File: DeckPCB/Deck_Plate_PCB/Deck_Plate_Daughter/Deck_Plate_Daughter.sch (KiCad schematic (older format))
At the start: 36 parts, among them J1 SunnyBuddy_Inhibit, J2 JST_Batt_Conn, J3 Motor_Inhibit, J4 BurnWire_Inhibit, J5 Power, J6 Raspberry_Pi_2_3, J7 Board_to_Board, Q1 Device_Q_NPN_BCE, U2 SunnyBuddy_Breakout, U3 Big_Easy_Driver, U4 TTL_Camera, U5 Adafruit_INA219_Breakout

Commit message: Started routing of Deck_Plate_PCB, the main board.
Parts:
- removed R4, R5: 10K, Resistor_THT:R_Axial_DIN0207_L6.3mm_D2.5mm_P10.16mm_Horizontal, symbol Device:R
- removed U4: TTL_Camera, Connector_PinHeader_2.54mm:PinHeader_1x04_P2.54mm_Vertical, symbol Deck_Plate_PCB:TTL_Camera
- J7: footprint Connector_PinHeader_2.54mm:PinHeader_1x07_P2.54mm_Vertical -> Connector_PinHeader_2.54mm:PinHeader_1x09_P2.54mm_Vertical; symbol Connector:Conn_01x07_Male -> Connector:Conn_01x09_Male
- Q1: value Device_Q_NPN_BCE -> BurnWire; symbol Deck_Plate_PCB-cache:Device_Q_NPN_BCE -> Deck_Plate_Daughter-rescue:Device_Q_NPN_BCE-Deck_Plate_PCB-cache
- U2: symbol Deck_Plate_PCB-cache:Deck_Plate_PCB_SunnyBuddy_Breakout -> Deck_Plate_Daughter-rescue:Deck_Plate_PCB_SunnyBuddy_Breakout-Deck_Plate_PCB-cache
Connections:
- net labels added: PayloadTemp, SCL, SDA, SolarArrayTemp
- net labels removed: 20(SDA), 21(SCL)
- wire segments 66 -> 59
- no-connect marks 20 -> 22
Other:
- note added: "BurnWire Circuitry"
- note added: "Inhibit Circuitry"
- note added: "RaspberryPI Interface"
- note added: "Signal and Power Board-to-Board Transfer"
- note added: "Solar Panel and Sensor Mangement"
- note removed: "TODO: Remove TTL camera back to other board and add 10k resistor connections to Arduino"
- moved on the sheet: D1, H15, H16, H17, H18, J1, J2, J3, J4, J5, J6, R1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

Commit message: Finised routing fro Main_Board, Daughter_Board, and BurnWire circuits. Creating SensorEndPanel board next.
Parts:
- removed Q1: BurnWire, Package_TO_SOT_THT:TO-251-3_Vertical, symbol Deck_Plate_Daughter-rescue:Device_Q_NPN_BCE-Deck_Plate_PCB-cache
- removed R2, R3: 4.7, Resistor_THT:R_Axial_DIN0207_L6.3mm_D2.5mm_P10.16mm_Horizontal, symbol Device:R
- J4: footprint Connector_PinHeader_2.54mm:PinHeader_1x02_P2.54mm_Vertical -> Connector_PinHeader_2.54mm:PinHeader_1x05_P2.54mm_Vertical; symbol Connector:Conn_01x02_Male -> Connector:Conn_01x05_Male
- J5: footprint Connector_PinHeader_2.54mm:PinHeader_1x03_P2.54mm_Vertical -> Connector_PinHeader_2.54mm:PinHeader_1x04_P2.54mm_Vertical; symbol Connector:Conn_01x03_Male -> Connector:Conn_01x04_Male
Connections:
- net Solar_IN- is gone; now on net GND: U2.1 (Solar_IN-)
- net 5V_Bus_1: now also J4.2 (Pin_2)
- net BurnWireSignal: now also J4.4 (Pin_4), J4.5 (Pin_5); no longer J4.2 (Pin_2)
- net GND: now also J1.3 (Pin_3), J4.3 (Pin_3), J5.4 (Pin_4); no longer J1.1 (Pin_1), J1.4 (Pin_4)
- net Sunny_Batt_Out: now also J1.1 (Pin_1), J1.4 (Pin_4); no longer J1.3 (Pin_3)
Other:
- note removed: "BurnWire Circuitry"
- moved on the sheet: J7
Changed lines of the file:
@@
 Wire Wire Line
 	1300 1200 1150 1200
-Text Label 1150 900  2    50   ~ 0
-Solar_IN-
 Text Label 1150 1000 2    50   ~ 0
 Solar_IN+
@@
 $EndComp
 Text Label 3000 1400 0    50   ~ 0
-5V_Bus_1
-$Comp
-L Deck_Plate_Daughter-rescue:Device_Q_NPN_BCE-Deck_Plate_PCB-cache Q1
-U 1 1 5E6100C5
-P 1450 3550
-F 0 "Q1" H 1641 3596 50  0000 L CNN
-F 1 "BurnWire" H 1641 3505 50  0000 L CNN
-F 2 "Package_TO_SOT_THT:TO-251-3_Vertical" H 1650 3650 50  0001 C CNN
-F 3 "" H 1450 3550 50  0001 C CNN
-	1    1450 3550
-	1    0    0    -1
-$EndComp
-$Comp
-L Device:R R2
-U 1 1 5E610D52
-P 1350 4000
-F 0 "R2" H 1420 4046 50  0000 L CNN
-F 1 "4.7" H 1420 3955 50  0000 L CNN
-F 2 "Resistor_THT:R_Axial_DIN0207_L6.3mm_D2.5mm_P10.16mm_Horizontal" V 1280 4000 50  0001 C CNN
-F 3 "~" H 1350 4000 50  0001 C CNN
-	1    1350 4000
-	1    0    0    -1
-$EndComp
-$Comp
-L Device:R R3
-U 1 1 5E611957
-P 1750 4000
-F 0 "R3" H 1820 4046 50  0000 L CNN
-F 1 "4.7" H 1820 3955 50  0000 L CNN
-F 2 "Resistor_THT:R_Axial_DIN0207_L6.3mm_D2.5mm_P10.16mm_Horizontal" V 1680 4000 50  0001 C CNN
-F 3 "~" H 1750 4000 50  0001 C CNN
-	1    1750 4000
-	1    0    0    -1
-$EndComp
-Wire Wire Line
-	1550 3750 1550 3850
-Wire Wire Line
-	1550 3850 1750 3850
-Wire Wire Line
-	1550 3850 1350 3850
-Connection ~ 1550 3850
-Wire Wire Line
-	1350 4150 1350 4200
-Wire Wire Line
-	1350 4200 1550 4200
-Wire Wire Line
-	1750 4200 1750 4150
-$Comp
-L power:GND #PWR0103
-U 1 1 5E61DCB1
-P 1550 4200
-F 0 "#PWR0103" H 1550 3950 50  0001 C CNN
-F 1 "GND" H 1555 4027 50  0000 C CNN
-F 2 "" H 1550 4200 50  0001 C CNN
-F 3 "" H 1550 4200 50  0001 C CNN
-	1    1550 4200
-	1    0    0    -1
-$EndComp
-Connection ~ 1550 4200
-Wire Wire Line
-	1550 4200 1750 4200
-Text Label 1250 3550 2    50   ~ 0
-BurnWireSignal
-Wire Wire Line
-	1550 3350 1550 3150
-Text Label 1550 3150 0    50   ~ 0
 5V_Bus_1
 $Comp
@@
 U 1 1 5E692559
 P 5500 950
-F 0 "J1" V 5800 1000 50  0000 L CNN
-F 1 "SunnyBuddy_Inhibit" V 5450 700 50  0000 L CNN
+F 0 "J1" V 5950 1100 50  0000 L CNN
+F 1 "SunnyBuddy_Inhibit" V 5450 600 50  0000 L CNN
 F 2 "Connector_PinHeader_2.54mm:PinHeader_1x04_P2.54mm_Vertical" H 5500 950 50  0001 C CNN
 F 3 "~" H 5500 950 50  0001 C CNN
@@
 $EndComp
 $Comp
-L power:GND #PWR0109
-U 1 1 5E693738
-P 5300 1150
-F 0 "#PWR0109" H 5300 900 50  0001 C CNN
-F 1 "GND" V 5305 1022 50  0000 R CNN
-F 2 "" H 5300 1150 50  0001 C CNN
-F 3 "" H 5300 1150 50  0001 C CNN
-	1    5300 1150
-	0    1    1    0
-$EndComp
-$Comp
 L power:GND #PWR0110
 U 1 1 5E693E04
-P 5600 1150
-F 0 "#PWR0110" H 5600 900 50  0001 C CNN
-F 1 "GND" V 5605 1022 50  0000 R CNN
-F 2 "" H 5600 1150 50  0001 C CNN
-F 3 "" H 5600 1150 50  0001 C CNN
-	1    5600 1150
-	0    -1   -1   0
+P 5400 1250
+F 0 "#PWR0110" H 5400 1000 50  0001 C CNN
+F 1 "GND" V 5405 1122 50  0000 R CNN
+F 2 "" H 5400 1250 50  0001 C CNN
+F 3 "" H 5400 1250 50  0001 C CNN
+	1    5400 1250
+	1    0    0    -1
 $EndComp
 Wire Wire Line
@@
 Wire Wire Line
 	5500 1150 5500 1250
-Text Label 5400 1250 3    50   ~ 0
+Text Label 5300 1250 3    50   ~ 0
 Sunny_Batt_Out
 Text Label 5500 1250 3    50   ~ 0
@@
 9V_Bus
 $Comp
-L Connector:Conn_01x02_Male J4
+L Connector:Conn_01x05_Male J4
 U 1 1 5E6B7185
 P 7750 950
-F 0 "J4" V 8100 1000 50  0000 L CNN
+F 0 "J4" V 8100 1350 50  0000 L CNN
 F 1 "BurnWire_Inhibit" V 7700 800 50  0000 L CNN
-F 2 "Connector_PinHeader_2.54mm:PinHeader_1x02_P2.54mm_Vertical" H 7750 950 50  0001 C CNN
+F 2 "Connector_PinHeader_2.54mm:PinHeader_1x05_P2.54mm_Vertical" H 7750 950 50  0001 C CNN
 F 3 "~" H 7750 950 50  0001 C CNN
 	1    7750 950
@@
 $EndComp
 Wire Wire Line
-	7650 1150 7650 1250
-Wire Wire Line
 	7750 1150 7750 1250
-Text Label 7650 1250 3    50   ~ 0
+Text Label 7550 1150 3    50   ~ 0
 BurnWireSignal
-Text Label 7750 1250 3    50   ~ 0
+Text Label 7650 1150 3    50   ~ 0
 BurnWireSignal
 $Comp
-L Connector:Conn_01x03_Male J5
+L Connector:Conn_01x04_Male J5
 U 1 1 5E6C52D2
-P 4100 3650
-F 0 "J5" H 4400 3500 50  0000 L CNN
-F 1 "Power" H 4050 3850 50  0000 L CNN
-F 2 "Connector_PinHeader_2.54mm:PinHeader_1x03_P2.54mm_Vertical" H 4100 3650 50  0001 C CNN
-F 3 "~" H 4100 3650 50  0001 C CNN
-	1    4100 3650
-	1    0    0    -1
-$EndComp
-Wire Wire Line
-	4300 3750 4400 3750
-Wire Wire Line
-	4300 3550 4400 3550
-Wire Wire Line
-	4300 3650 4400 3650
-Text Label 4400 3550 0    50   ~ 0
+P 750 4500
+F 0 "J5" H 750 4200 50  0000 L CNN
+F 1 "Power" H 700 4700 50  0000 L CNN
+F 2 "Connector_PinHeader_2.54mm:PinHeader_1x04_P2.54mm_Vertical" H 750 4500 50  0001 C CNN
+F 3 "~" H 750 4500 50  0001 C CNN
+	1    750  4500
+	1    0    0    -1
+$EndComp
+Wire Wire Line
+	950  4600 1050 4600
+Wire Wire Line
+	950  4400 1050 4400
+Wire Wire Line
+	950  4500 1050 4500
+Text Label 1050 4400 0    50   ~ 0
 5V_Bus_1
-Text Label 4400 3650 0    50   ~ 0
+Text Label 1050 4500 0    50   ~ 0
 9V_Bus
-Text Label 4400 3750 0    50   ~ 0
+Text Label 1050 4600 0    50   ~ 0
 5V_Bus_2
 $Comp
@@
 L Connector:Conn_01x09_Male J7
 U 1 1 5EDC5910
-P 4100 2850
-F 0 "J7" H 4450 2400 50  0000 C CNN
-F 1 "Board_to_Board" H 4350 3400 50  0000 C CNN
-F 2 "Connector_PinHeader_2.54mm:PinHeader_1x09_P2.54mm_Vertical" H 4100 2850 50  0001 C CNN
-F 3 "~" H 4100 2850 50  0001 C CNN
-	1    4100 2850
-	1    0    0    -1
-$EndComp
-Wire Wire Line
-	4300 2650 4400 2650
-Wire Wire Line
-	4300 2750 4400 2750
-Wire Wire Line
-	4300 2850 4400 2850
-Wire Wire Line
-	4300 2950 4400 2950
-Wire Wire Line
-	4300 3050 4400 3050
-Text Label 4400 2650 0    50   ~ 0
+P 750 3700
+F 0 "J7" H 1100 3250 50  0000 C CNN
+F 1 "Board_to_Board" H 1000 4250 50  0000 C CNN
+F 2 "Connector_PinHeader_2.54mm:PinHeader_1x09_P2.54mm_Vertical" H 750 3700 50  0001 C CNN
+F 3 "~" H 750 3700 50  0001 C CNN
+	1    750  3700
+	1    0    0    -1
+$EndComp
+Wire Wire Line
+	950  3500 1050 3500
+Wire Wire Line
+	950  3600 1050 3600
+Wire Wire Line
+	950  3700 1050 3700
+Wire Wire Line
+	950  3800 1050 3800
+Wire Wire Line
+	950  3900 1050 3900
+Text Label 1050 3500 0    50   ~ 0
 TTL_TX
-Text Label 4400 2750 0    50   ~ 0
+Text Label 1050 3600 0    50   ~ 0
 TTL_RX
-Text Label 4400 2850 0    50   ~ 0
+Text Label 1050 3700 0    50   ~ 0
 BurnWireSignal
-Text Label 4400 2950 0    50   ~ 0
+Text Label 1050 3800 0    50   ~ 0
 Step
-Text Label 4400 3050 0    50   ~ 0
+Text Label 1050 3900 0    50   ~ 0
 Dir
 Wire Wire Line
-	4300 3150 4400 3150
-Wire Wire Line
-	4300 2550 4400 2550
-Text Label 4400 2450 0    50   ~ 0
+	950  4000 1050 4000
+Wire Wire Line
+	950  3400 1050 3400
+Text Label 1050 3300 0    50   ~ 0
 SDA
-Text Label 4400 2550 0    50   ~ 0
+Text Label 1050 3400 0    50   ~ 0
 SCL
 $Comp
@@
 $EndComp
 Wire Wire Line
-	4300 2450 4400 2450
-Wire Wire Line
-	4300 3250 4400 3250
-Text Label 4400 3150 0    50   ~ 0
+	950  3300 1050 3300
+Wire Wire Line
+	950  4100 1050 4100
+Text Label 1050 4000 0    50   ~ 0
 SolarArrayTemp
-Text Label 4400 3250 0    50   ~ 0
+Text Label 1050 4100 0    50   ~ 0
 PayloadTemp
 NoConn ~ 8900 1350
 NoConn ~ 8900 1450
-Wire Notes Line
-	500  2850 3800 2850
-Wire Notes Line
-	3800 500  3800 4500
 Wire Notes Line
 	3850 2000 8250 2000
@@
 Text Notes 550  650  0    79   Italic 16
 Solar Panel and Sensor Mangement
-Text Notes 500  3000 0    79   Italic 16
-BurnWire Circuitry
-Text Notes 3850 2200 0    79   Italic 16
+Text Notes 500  3050 0    79   Italic 16
 Signal and Power Board-to-Board Transfer
-Wire Notes Line
-	500  4500 8250 4500
-Wire Notes Line
-	8250 500  8250 4500
 Text Notes 8350 650  0    79   Italic 16
 RaspberryPI Interface
+Wire Notes Line
+	500  2850 3800 2850
+Wire Notes Line
+	3800 2850 3800 500
+$Comp
+L power:GND #PWR0103
+U 1 1 5E687FD9
+P 1150 900
+F 0 "#PWR0103" H 1150 650 50  0001 C CNN
+F 1 "GND" V 1155 772 50  0000 R CNN
+F 2 "" H 1150 900 50  0001 C CNN
+F 3 "" H 1150 900 50  0001 C CNN
+	1    1150 900
+	0    1    1    0
+$EndComp
+Wire Wire Line
+	5300 1150 5300 1250
+Text Label 5600 1350 3    50   ~ 0
+Sunny_Batt_Out
+Wire Wire Line
+	5600 1150 5600 1350
+$Comp
+L power:GND #PWR0106
+U 1 1 5E69FEA7
+P 950 4700
+F 0 "#PWR0106" H 950 4450 50  0001 C CNN
+F 1 "GND" H 955 4527 50  0000 C CNN
+F 2 "" H 950 4700 50  0001 C CNN
+F 3 "" H 950 4700 50  0001 C CNN
+	1    950  4700
+	0    -1   -1   0
+$EndComp
+$Comp
+L power:GND #PWR?
+U 1 1 5E6EFB98
+P 7750 1250
+F 0 "#PWR?" H 7750 1000 50  0001 C CNN
+F 1 "GND" V 7755 1122 50  0000 R CNN
+F 2 "" H 7750 1250 50  0001 C CNN
+F 3 "" H 7750 1250 50  0001 C CNN
+	1    7750 1250
+	1    0    0    -1
+$EndComp
+Text Label 7850 1150 3    50   ~ 0
+5V_Bus_1
+Text Label 7950 1150 3    50   ~ 0
+BurnWireSignal
 $EndSCHEMATC

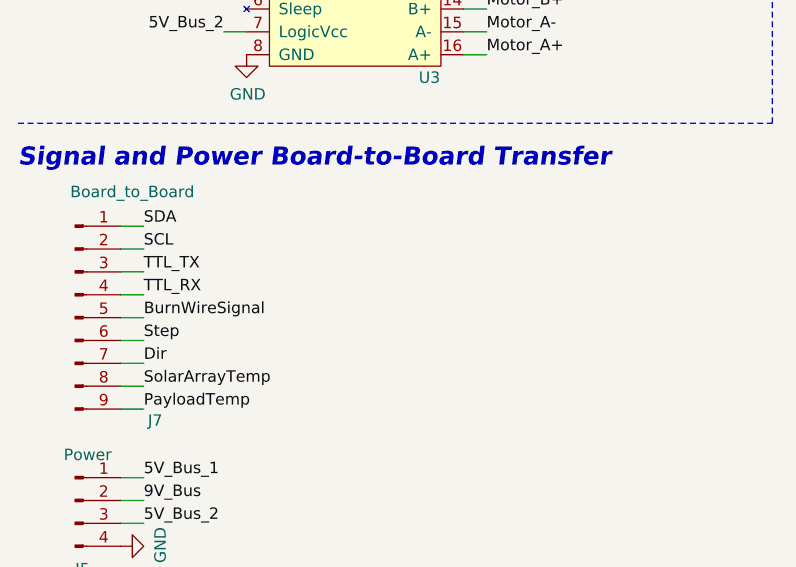
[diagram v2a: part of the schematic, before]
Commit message: updated PCB routing and creation of BurnWire circuit board and updated Daughter_Board
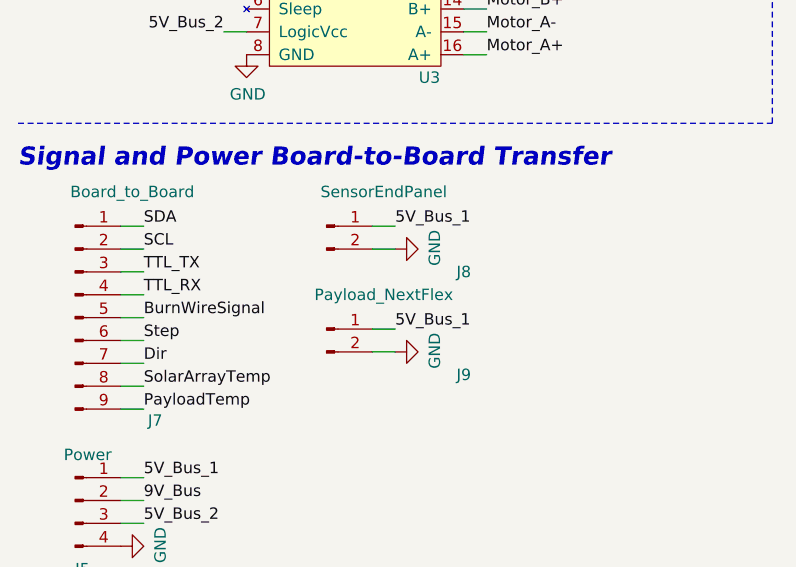
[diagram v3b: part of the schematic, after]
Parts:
- added J8: SensorEndPanel, Connector_PinHeader_2.54mm:PinHeader_1x02_P2.54mm_Vertical, symbol Connector:Conn_01x02_Male
- added J9: Payload_NextFlex, Connector_PinHeader_2.54mm:PinHeader_1x02_P2.54mm_Vertical, symbol Connector:Conn_01x02_Male
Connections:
- net 5V_Bus_1: now also J8.1 (Pin_1), J9.1 (Pin_1)
- net GND: now also J8.2 (Pin_2), J9.2 (Pin_2)
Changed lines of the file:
@@
 $EndComp
 $Comp
-L power:GND #PWR?
+L power:GND #PWR0107
 U 1 1 5E6EFB98
 P 7750 1250
-F 0 "#PWR?" H 7750 1000 50  0001 C CNN
+F 0 "#PWR0107" H 7750 1000 50  0001 C CNN
 F 1 "GND" V 7755 1122 50  0000 R CNN
 F 2 "" H 7750 1250 50  0001 C CNN
@@
 Text Label 7950 1150 3    50   ~ 0
 BurnWireSignal
+$Comp
+L Connector:Conn_01x02_Male J8
+U 1 1 5E6215D5
+P 1850 3300
+F 0 "J8" H 2450 3100 50  0000 C CNN
+F 1 "SensorEndPanel" H 2100 3450 50  0000 C CNN
+F 2 "Connector_PinHeader_2.54mm:PinHeader_1x02_P2.54mm_Vertical" H 1850 3300 50  0001 C CNN
+F 3 "~" H 1850 3300 50  0001 C CNN
+	1    1850 3300
+	1    0    0    -1
+$EndComp
+Wire Wire Line
+	2050 3300 2150 3300
+Wire Wire Line
+	2050 3400 2150 3400
+Text Label 2150 3300 0    50   ~ 0
+5V_Bus_1
+$Comp
+L power:GND #PWR0108
+U 1 1 5E6261E7
+P 2150 3400
+F 0 "#PWR0108" H 2150 3150 50  0001 C CNN
+F 1 "GND" H 2155 3227 50  0000 C CNN
+F 2 "" H 2150 3400 50  0001 C CNN
+F 3 "" H 2150 3400 50  0001 C CNN
+	1    2150 3400
+	0    -1   -1   0
+$EndComp
+$Comp
+L Connector:Conn_01x02_Male J9
+U 1 1 5E62AB42
+P 1850 3750
+F 0 "J9" H 2450 3550 50  0000 C CNN
+F 1 "Payload_NextFlex" H 2100 3900 50  0000 C CNN
+F 2 "Connector_PinHeader_2.54mm:PinHeader_1x02_P2.54mm_Vertical" H 1850 3750 50  0001 C CNN
+F 3 "~" H 1850 3750 50  0001 C CNN
+	1    1850 3750
+	1    0    0    -1
+$EndComp
+Wire Wire Line
+	2050 3750 2150 3750
+Wire Wire Line
+	2050 3850 2150 3850
+Text Label 2150 3750 0    50   ~ 0
+5V_Bus_1
+$Comp
+L power:GND #PWR0109
+U 1 1 5E62DFA6
+P 2150 3850
+F 0 "#PWR0109" H 2150 3600 50  0001 C CNN
+F 1 "GND" H 2155 3677 50  0000 C CNN
+F 2 "" H 2150 3850 50  0001 C CNN
+F 3 "" H 2150 3850 50  0001 C CNN
+	1    2150 3850
+	0    -1   -1   0
+$EndComp
 $EndSCHEMATC

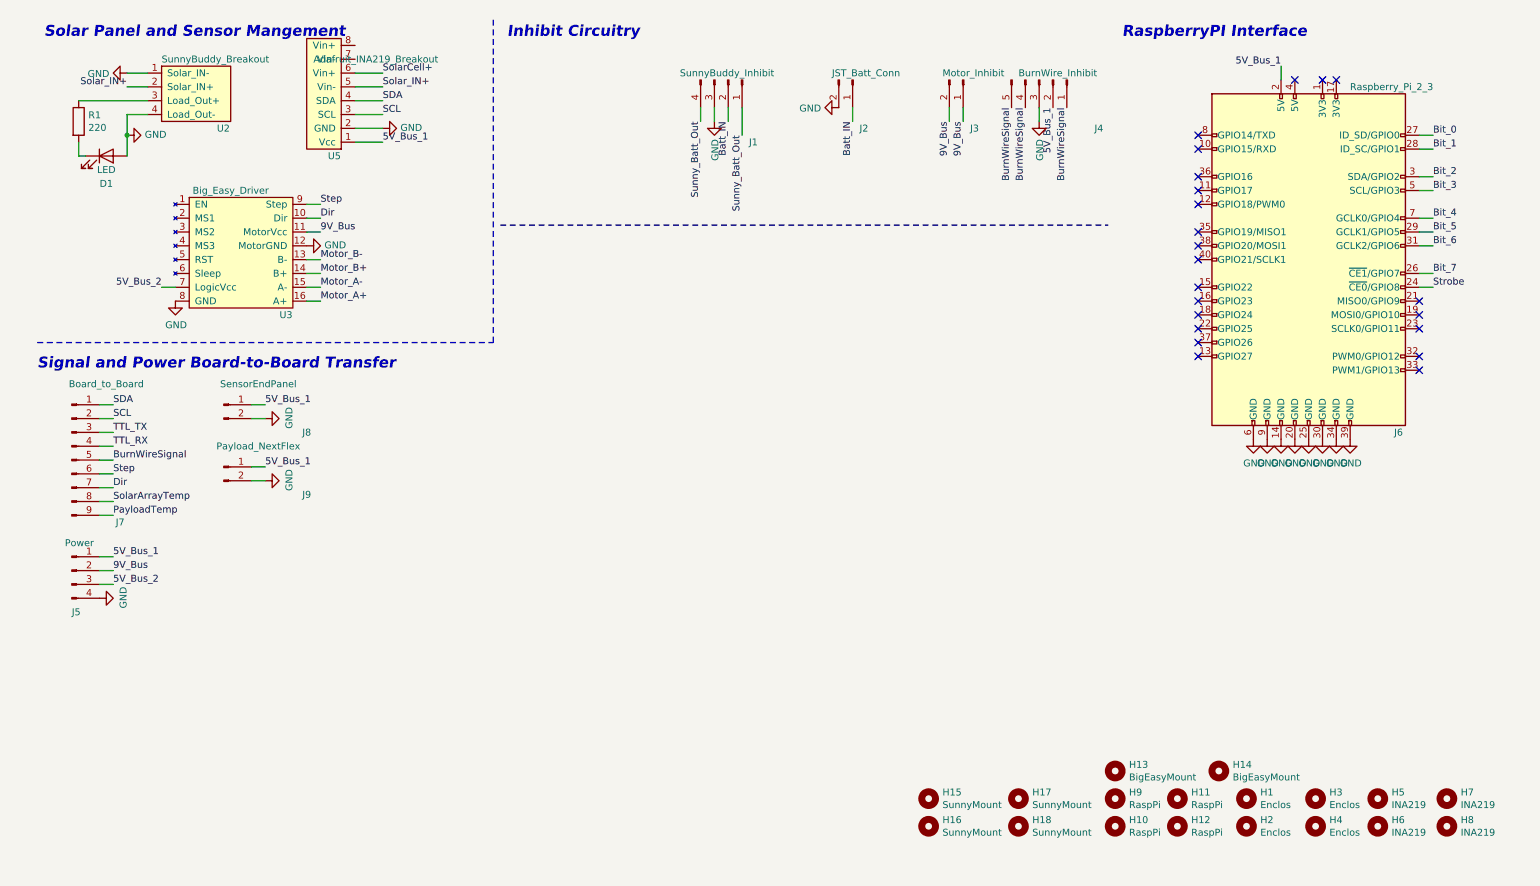
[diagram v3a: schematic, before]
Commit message: Updated PCB for NASA analog lines and signal conditioning circuitry. Added Gerber file ZIP for DECK_PLATE_MAIN
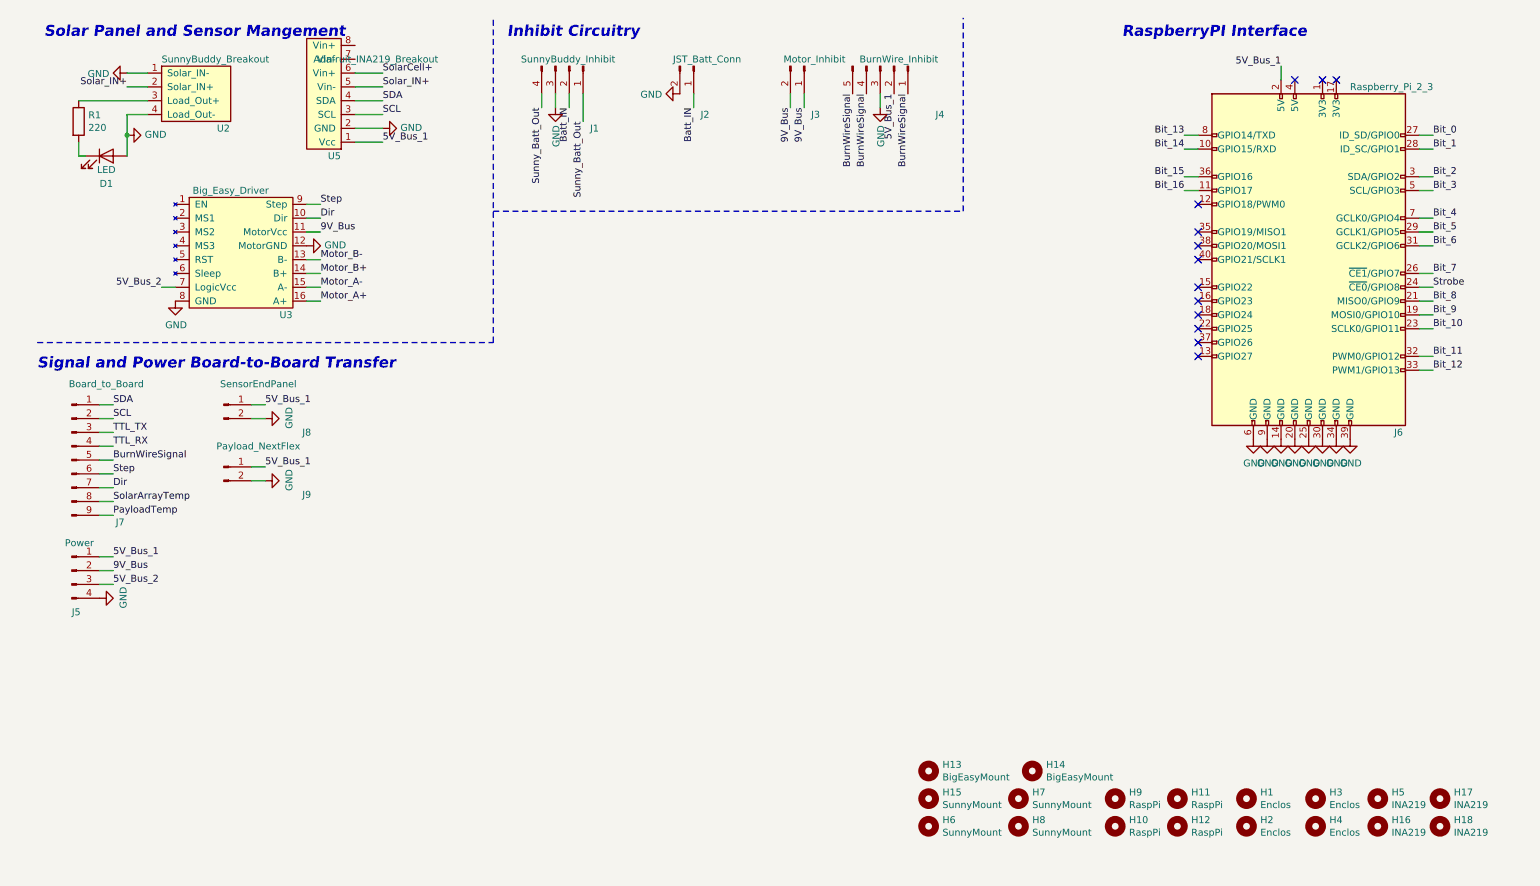
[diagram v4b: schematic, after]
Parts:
- H13, H14: footprint MountingHole:MountingHole_3.2mm_M3 -> Deck_Plate_PCB:BigEasy_MountingHole_3.2mm_M3
- H15, H5: footprint MountingHole:MountingHole_2.5mm -> Deck_Plate_PCB:Accel_MountingHole_2.5mm
- H16, H17, H18: value SunnyMount -> INA219; footprint MountingHole:MountingHole_2.5mm -> Deck_Plate_PCB:Accel_MountingHole_2.5mm
- H6, H7, H8: value INA219 -> SunnyMount; footprint MountingHole:MountingHole_2.5mm -> Deck_Plate_PCB:Accel_MountingHole_2.5mm
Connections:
- net Bit_14: now reaches J6.10 (GPIO15/RXD)
- net Bit_16: now reaches J6.11 (GPIO17)
- net Bit_9: now reaches J6.19 (MOSI0/GPIO10)
- net Bit_8: now reaches J6.21 (MISO0/GPIO9)
- net Bit_10: now reaches J6.23 (SCLK0/GPIO11)
- net Bit_11: now reaches J6.32 (PWM0/GPIO12)
- net Bit_12: now reaches J6.33 (PWM1/GPIO13)
- net Bit_15: now reaches J6.36 (GPIO16)
- net Bit_13: now reaches J6.8 (GPIO14/TXD)
- no-connect marks 22 -> 13
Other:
- moved on the sheet: H13, J1, J2, J3, J4
